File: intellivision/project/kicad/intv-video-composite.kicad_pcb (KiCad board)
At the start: 2 copper layers, 35.5 x 33.5 mm, 21 parts, among them J1 VID IN, J2 VID OUT, J3 AUD IN, J4 AUD OUT, J5 +5V IN, J6 GND IN, J7 GND OUT, Q1 2N3904, Q2 2N3904

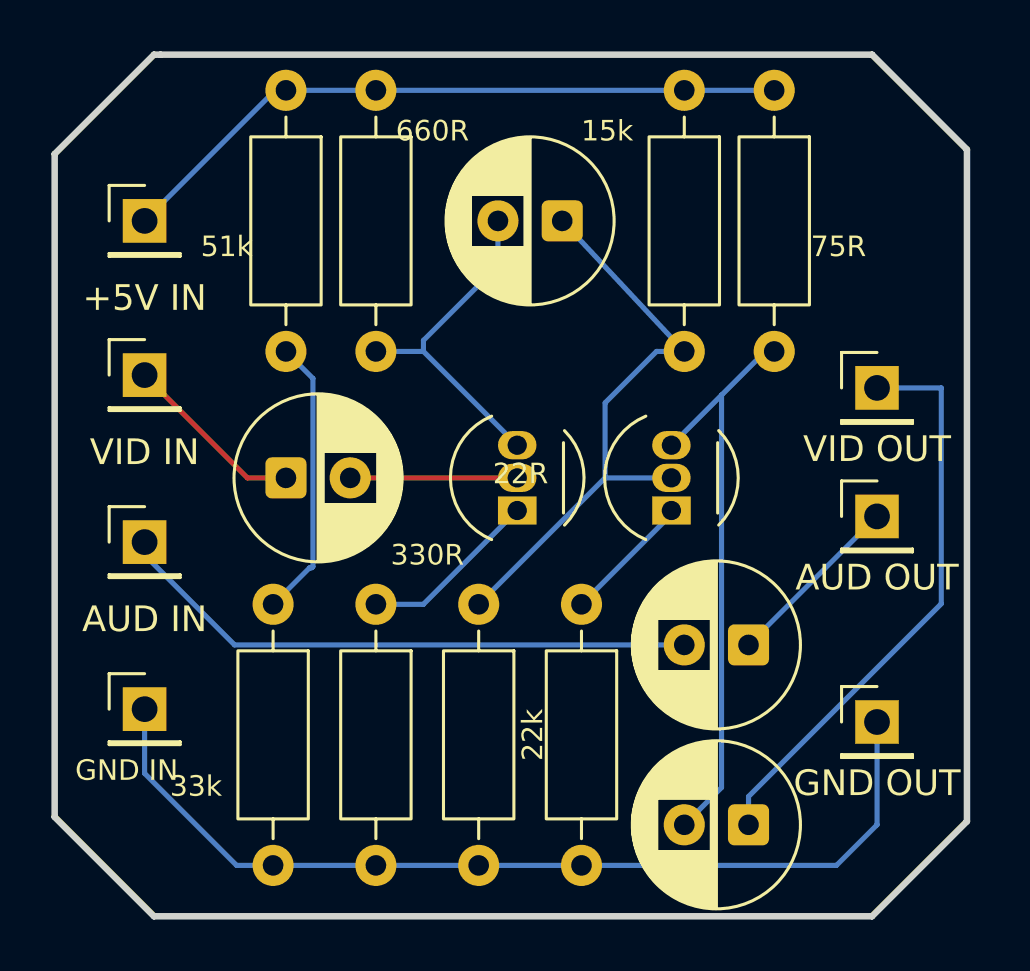
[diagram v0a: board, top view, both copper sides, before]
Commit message: Rename Intellivision composite production set
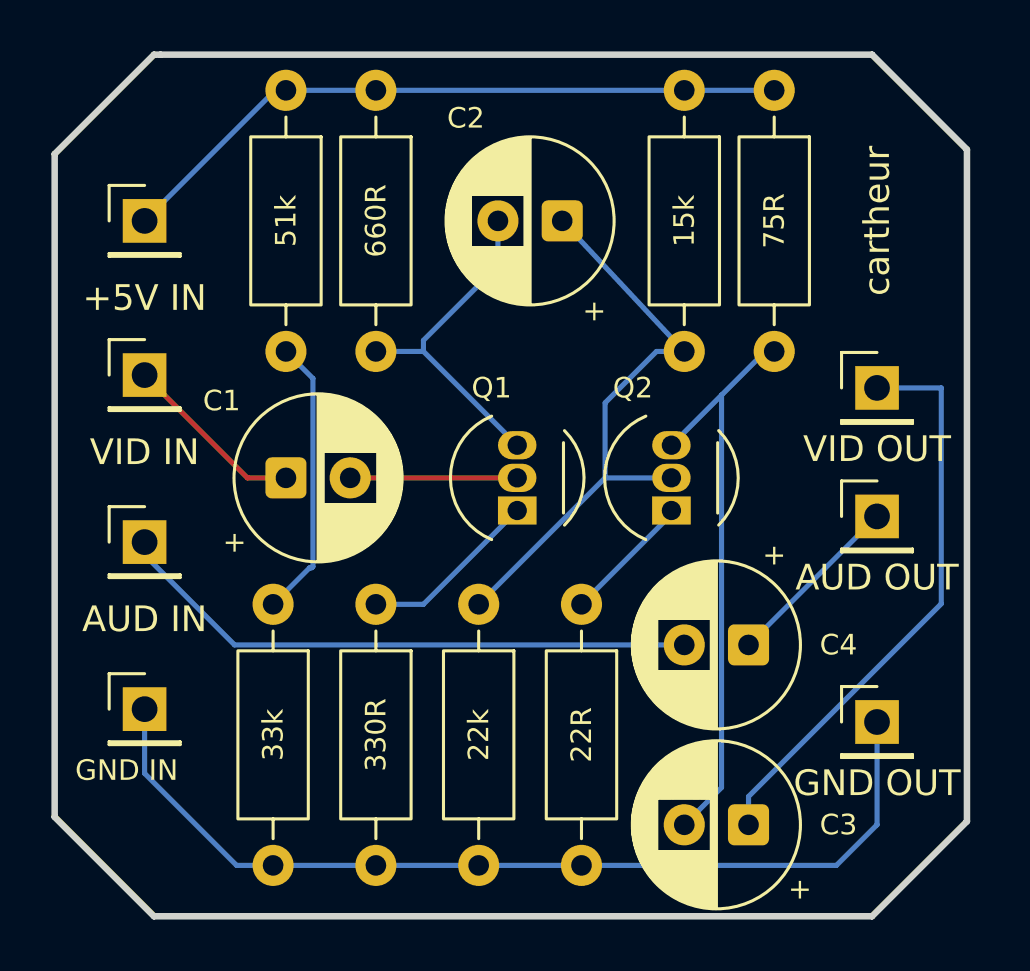
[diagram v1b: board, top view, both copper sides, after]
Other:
- board text added: "+"
- board text added: "C1"
- board text added: "C2"
- board text added: "C3"
- board text added: "C4"
- board text added: "E B C"
- board text added: "Q1"
- board text added: "Q2"
- board text added: "cartheur"

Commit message: Update to rev.1
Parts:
- J1, J2, J3, J4, J5, J6, J7: footprint Connector_PinHeader_2.54mm:PinHeader_1x01_P2.54mm_Vertical -> Intellivision:WirePad_1x01_D3.5mm_Drill1.3mm
- moved J2 1.00 mm to (99.0, 77.5)
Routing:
- net Net-(J2-Pin_1): track 22.6 -> 24.0 mm
